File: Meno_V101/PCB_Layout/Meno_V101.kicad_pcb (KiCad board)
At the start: 2 copper layers, 68.5 x 57.8 mm, 51 parts, among them J1 5077CR-16SMC2, J10 Conn_02x12, J2 AVR-ISP-6, J3 18742, J4 Conn_01x08, J5 Conn_01x10, J6 Conn_01x19, J7 Conn_01x06, J8 Conn_01x08, J9 Conn_01x15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

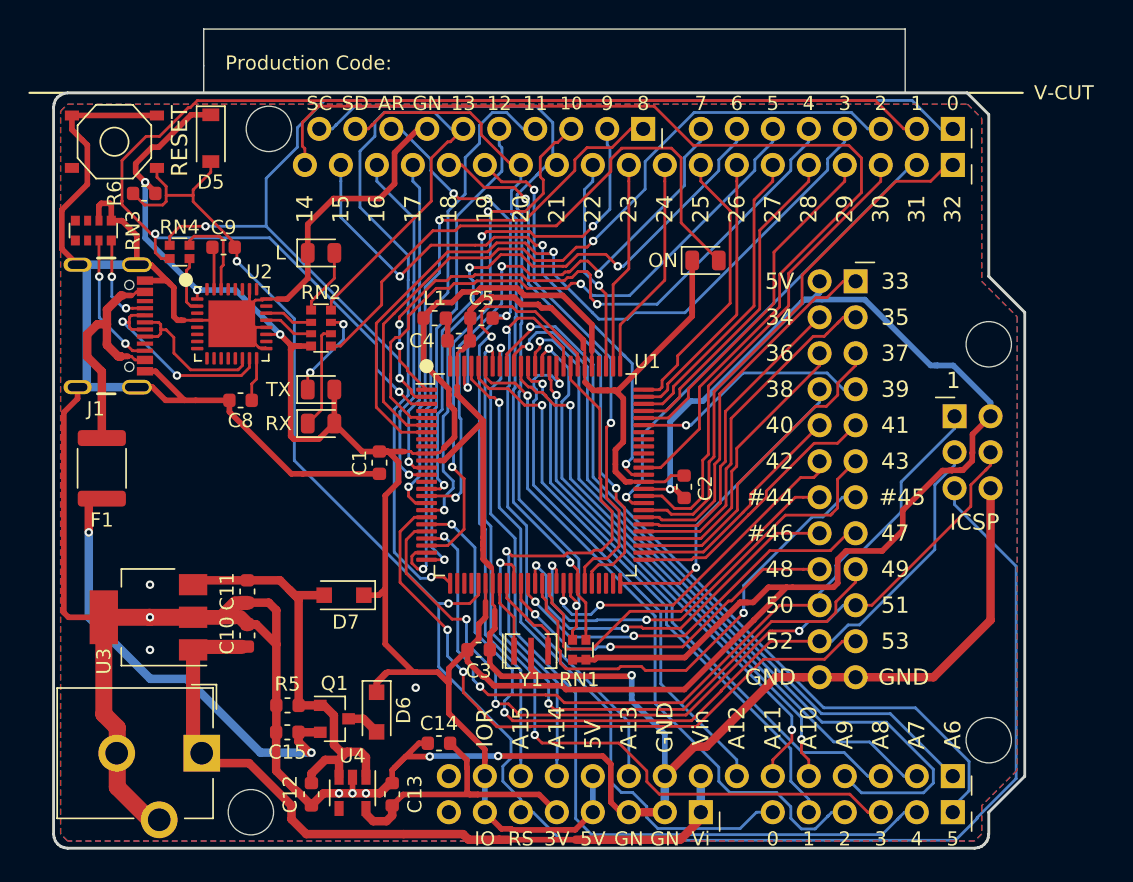
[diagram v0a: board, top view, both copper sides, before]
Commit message: プリント基板のパターンとシルク位置の変更
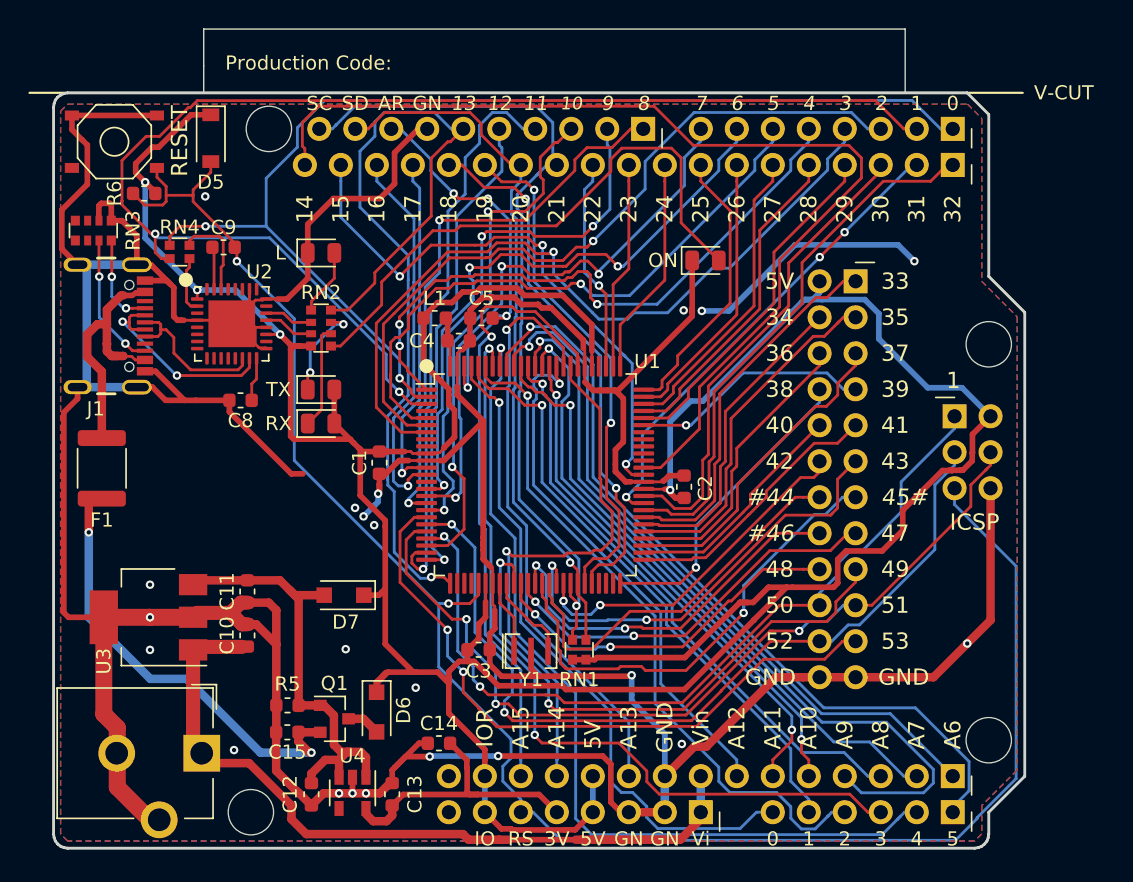
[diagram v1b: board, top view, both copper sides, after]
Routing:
- net GND: track 351.8 -> 369.7 mm, vias 10 -> 22
- net D16: track 24.9 -> 27.9 mm
- net D17: track 22.9 -> 24.4 mm
- net +5V: track 246.7 -> 248.0 mm
- net D13: track 61.5 -> 62.6 mm
- net VBUS: track 18.4 -> 19.4 mm
- net D8: track 39.4 -> 40.4 mm
- net D32: track 37.5 -> 38.0 mm
- net D31: vias 1 -> 3
